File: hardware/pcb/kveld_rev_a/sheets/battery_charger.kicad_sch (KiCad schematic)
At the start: 0 parts

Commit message: feat(hw): capture rev a schematic and refine enclosure
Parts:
- added C4: 1uF 25V, Capacitor_SMD:C_0603_1608Metric, symbol Device:C
- added C5: 10uF 25V, Capacitor_SMD:C_0805_2012Metric, symbol Device:C
- added C6: 1uF 10V, Capacitor_SMD:C_0603_1608Metric, symbol Device:C
- added C7: 100nF, Capacitor_SMD:C_0603_1608Metric, symbol Device:C
- added J3: Protected LiPo + NTC, Connector_JST:JST_PH_S3B-PH-SM4-TB_1x03-1MP_P2.00mm_Horizontal, symbol Connector_Generic:Conn_01x03
- added R10, R9: 10k, Resistor_SMD:R_0603_1608Metric, symbol Device:R
- added R11: 1M, Resistor_SMD:R_0603_1608Metric, symbol Device:R
- added R12: 470k, Resistor_SMD:R_0603_1608Metric, symbol Device:R
- added R13: 100k, Resistor_SMD:R_0603_1608Metric, symbol Device:R
- added R7: 18k, Resistor_SMD:R_0603_1608Metric, symbol Device:R
- added R8: 1.20k, Resistor_SMD:R_0603_1608Metric, symbol Device:R
- added U2: BQ25185DLH, Package_DFN_QFN:Texas_DLH0010A_WSON-10-1EP_2.2x2mm_P0.4mm_EP0.9x1.5mm_ThermalVias, symbol Kveld:BQ25185DLH
- added U5: TPS22917DBVR, Package_TO_SOT_SMD:SOT-23-6, symbol Power_Management:TPS22917DBV
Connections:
- new net 3V3: R10.1, R9.1
- new net BAT_NTC: J3.2 (Pin_2), U2.6 (TS/MR)
- new net BQ_ISET: R8.1, U2.8 (ISET)
- new net BQ_VSET: R7.1, U2.7 (ILIM/VSET)
- new net CHG_ENABLE: R13.1, U2.4 (~{CE})
- new net CHG_STAT1: R9.2, U2.9 (STAT1)
- new net CHG_STAT2: R10.2, U2.3 (STAT2)
- new net GND: C4.2, C5.2, C6.2, C7.2, J3.3 (Pin_3), R12.2, R13.2, R7.2, R8.2, U2.11 (EP), U2.5 (GND), U5.2 (GND)
- new net USB_VBUS: C4.1, U2.10 (IN)
- new net VBAT: C6.1, J3.1 (Pin_1), U2.2 (BAT), U5.1 (VIN)
- new net VBAT_DIV_IN: R11.1, U5.6 (VOUT)
- new net VBAT_SENSE: C7.1, R11.2, R12.1
- new net VBAT_SENSE_EN: U5.3 (ON)
- new net VSYS: C5.1, U2.1 (SYS)
- no-connect marks 0 -> 2
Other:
- note added: "BQ25185: 4.2 V cell, 500 mA USB limit, 250 mA charge. Pack must include PCM and 10 kΩ NTC."
- title: (none) -> Battery charger, protected pack, and measurements

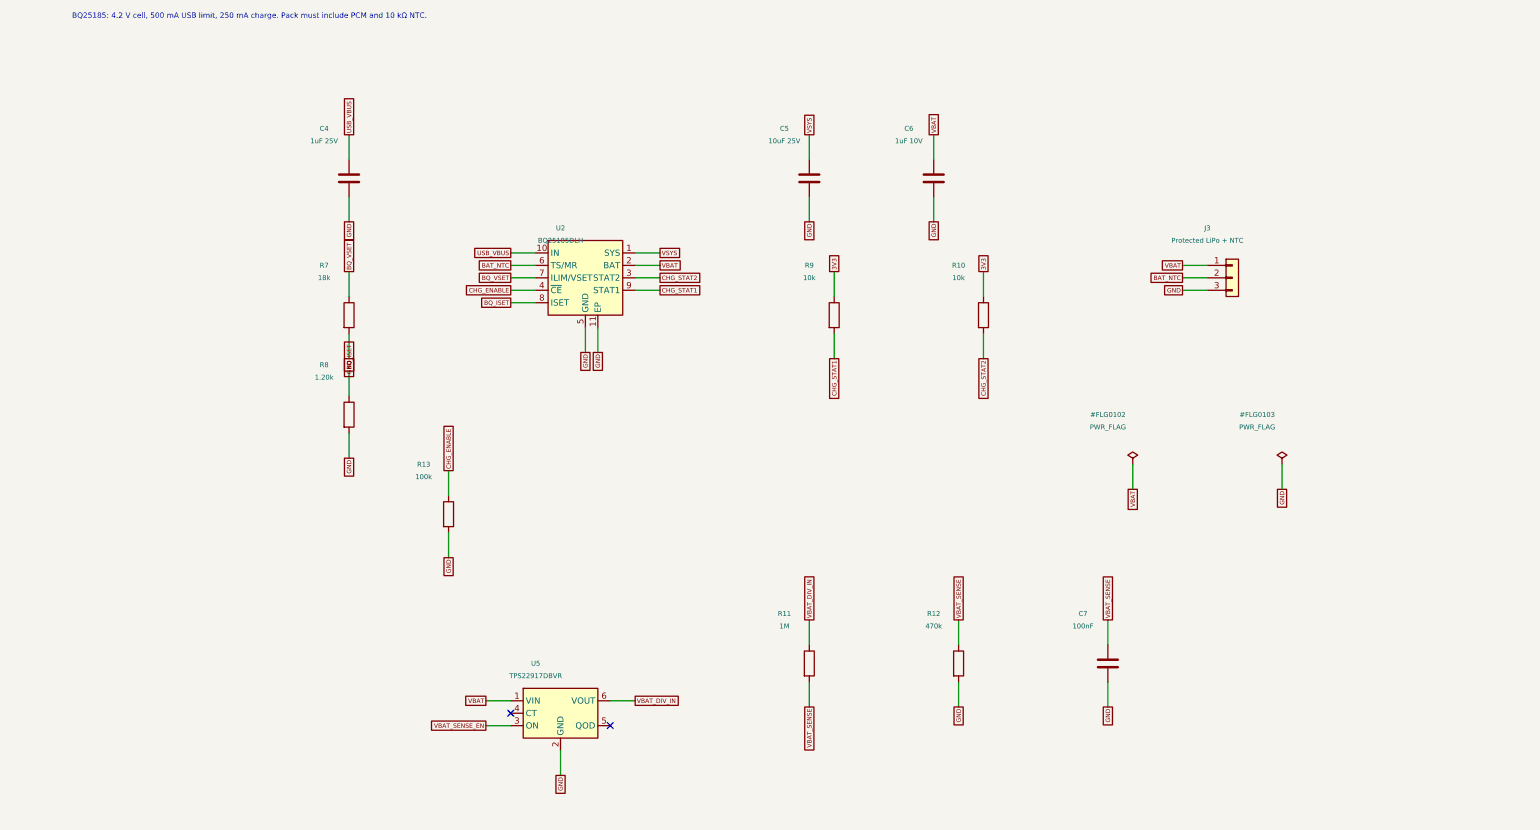
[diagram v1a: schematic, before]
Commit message: refactor(hw): consolidate and clarify schematic
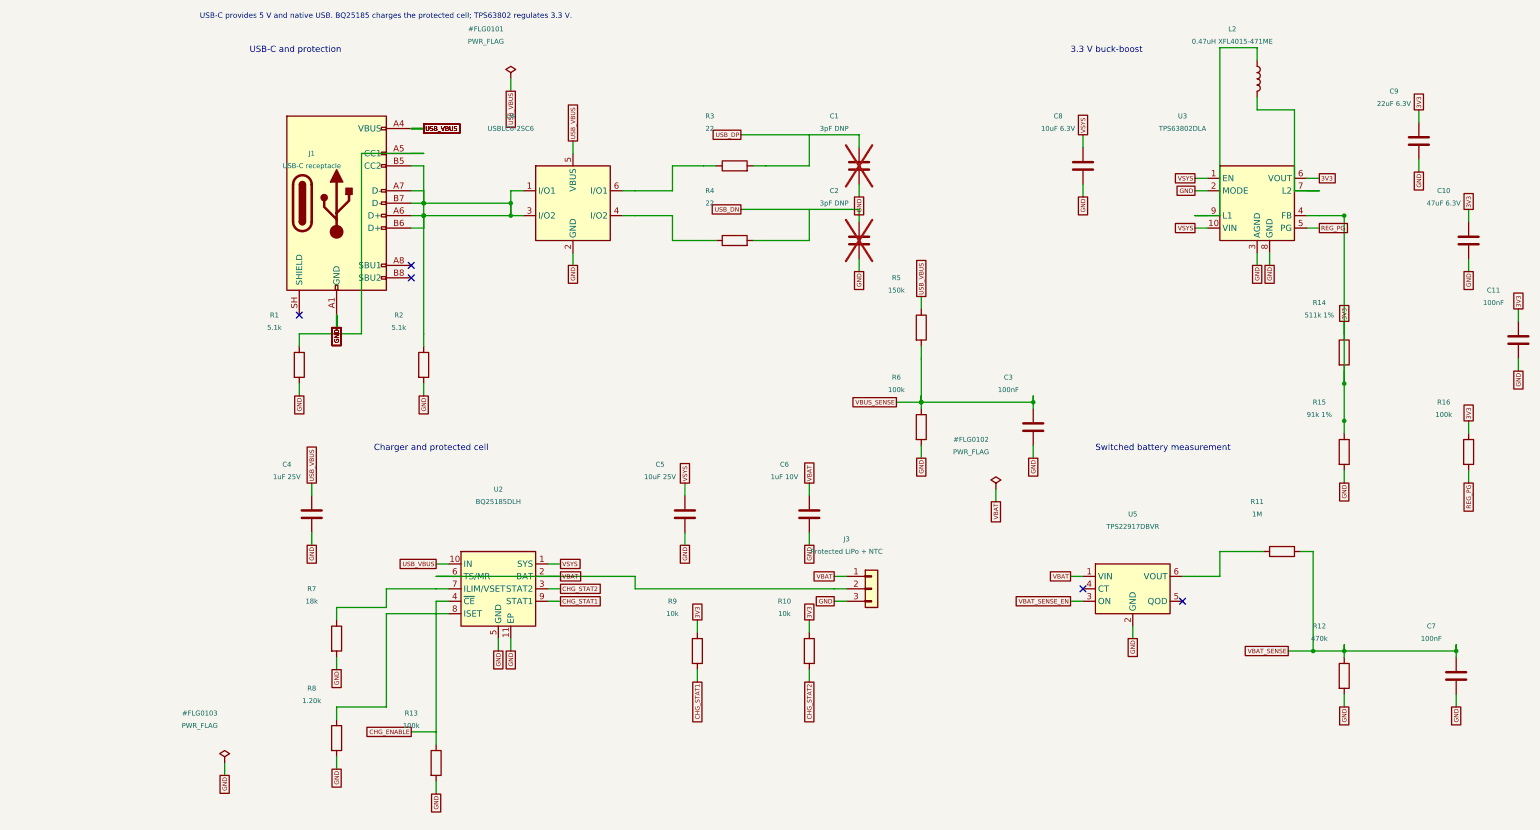
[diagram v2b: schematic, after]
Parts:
- added C1, C2: 3pF DNP, Capacitor_SMD:C_0603_1608Metric, symbol Device:C
- added C10: 47uF 6.3V, Capacitor_SMD:C_0805_2012Metric, symbol Device:C
- added C11, C3: 100nF, Capacitor_SMD:C_0603_1608Metric, symbol Device:C
- added C8: 10uF 6.3V, Capacitor_SMD:C_0603_1608Metric, symbol Device:C
- added C9: 22uF 6.3V, Capacitor_SMD:C_0603_1608Metric, symbol Device:C
- added J1: USB-C receptacle, Connector_USB:USB_C_Receptacle_HRO_TYPE-C-31-M-12, symbol Connector:USB_C_Receptacle_USB2.0_16P
- added L2: 0.47uH XFL4015-471ME, symbol Device:L
- added R1, R2: 5.1k, Resistor_SMD:R_0603_1608Metric, symbol Device:R
- added R14: 511k 1%, Resistor_SMD:R_0603_1608Metric, symbol Device:R
- added R15: 91k 1%, Resistor_SMD:R_0603_1608Metric, symbol Device:R
- added R16, R6: 100k, Resistor_SMD:R_0603_1608Metric, symbol Device:R
- added R3, R4: 22, Resistor_SMD:R_0603_1608Metric, symbol Device:R
- added R5: 150k, Resistor_SMD:R_0603_1608Metric, symbol Device:R
- added U3: TPS63802DLA, symbol Kveld:TPS63802DLA
- added U4: USBLC6-2SC6, Package_TO_SOT_SMD:SOT-23-6, symbol Kveld:USBLC6-2SC6
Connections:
- net BAT_NTC is gone; now on net VBAT: J3.2 (Pin_2), U2.6 (TS/MR)
- net 3V3: now also C10.1, C11.1, C9.1, R14.1, R14.2, R15.1, R16.1, U3.4 (FB), U3.6 (VOUT)
- net GND: now also C1.2, C10.2, C11.2, C2.2, C3.2, C8.2, C9.2, J1.A1 (GND), J1.A12 (GND), J1.B1 (GND), J1.B12 (GND), R1.2, R15.2, R2.2, R6.2, U3.2 (MODE), U3.3 (AGND), U3.8 (GND), U4.2 (GND)
- net USB_VBUS: now also J1.A4 (VBUS), J1.A9 (VBUS), J1.B4 (VBUS), J1.B9 (VBUS), R5.1, U4.5 (VBUS)
- net VSYS: now also C8.1, U3.1 (EN), U3.10 (VIN)
- net BQ_ISET: no longer names the net of R8.1, U2.8 (ISET)
- net BQ_VSET: no longer names the net of R7.1, U2.7 (ILIM/VSET)
- net VBAT_DIV_IN: no longer names the net of R11.1, U5.6 (VOUT)
- new net: R4.1, U4.4 (I/O2)
- new net: R3.1, U4.6 (I/O1)
- new net: L2.1, U3.9 (L1)
- new net: L2.2, U3.7 (L2)
- new net: J1.A5 (CC1), R1.1
- new net: J1.A6 (D+), J1.A7 (D-), J1.B5 (CC2), J1.B6 (D+), J1.B7 (D-), R2.1, U4.1 (I/O1), U4.3 (I/O2)
- new net REG_PG: R16.2, U3.5 (PG)
- new net USB_DN: C2.1, R4.2
- new net USB_DP: C1.1, R3.2
- new net VBUS_SENSE: C3.1, R5.2, R6.1
- no-connect marks 2 -> 5
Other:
- note added: "3.3 V buck-boost"
- note added: "Charger and protected cell"
- note added: "Switched battery measurement"
- note added: "USB-C and protection"
- note added: "USB-C provides 5 V and native USB. BQ25185 charges the protected cell; TPS63802 regulates 3.3 V."
- note removed: "BQ25185: 4.2 V cell, 500 mA USB limit, 250 mA charge. Pack must include PCM and 10 kΩ NTC."
- title: Battery charger, protected pack, and measurements -> Power, charging, and USB

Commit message: fix(hw): use native ground symbols
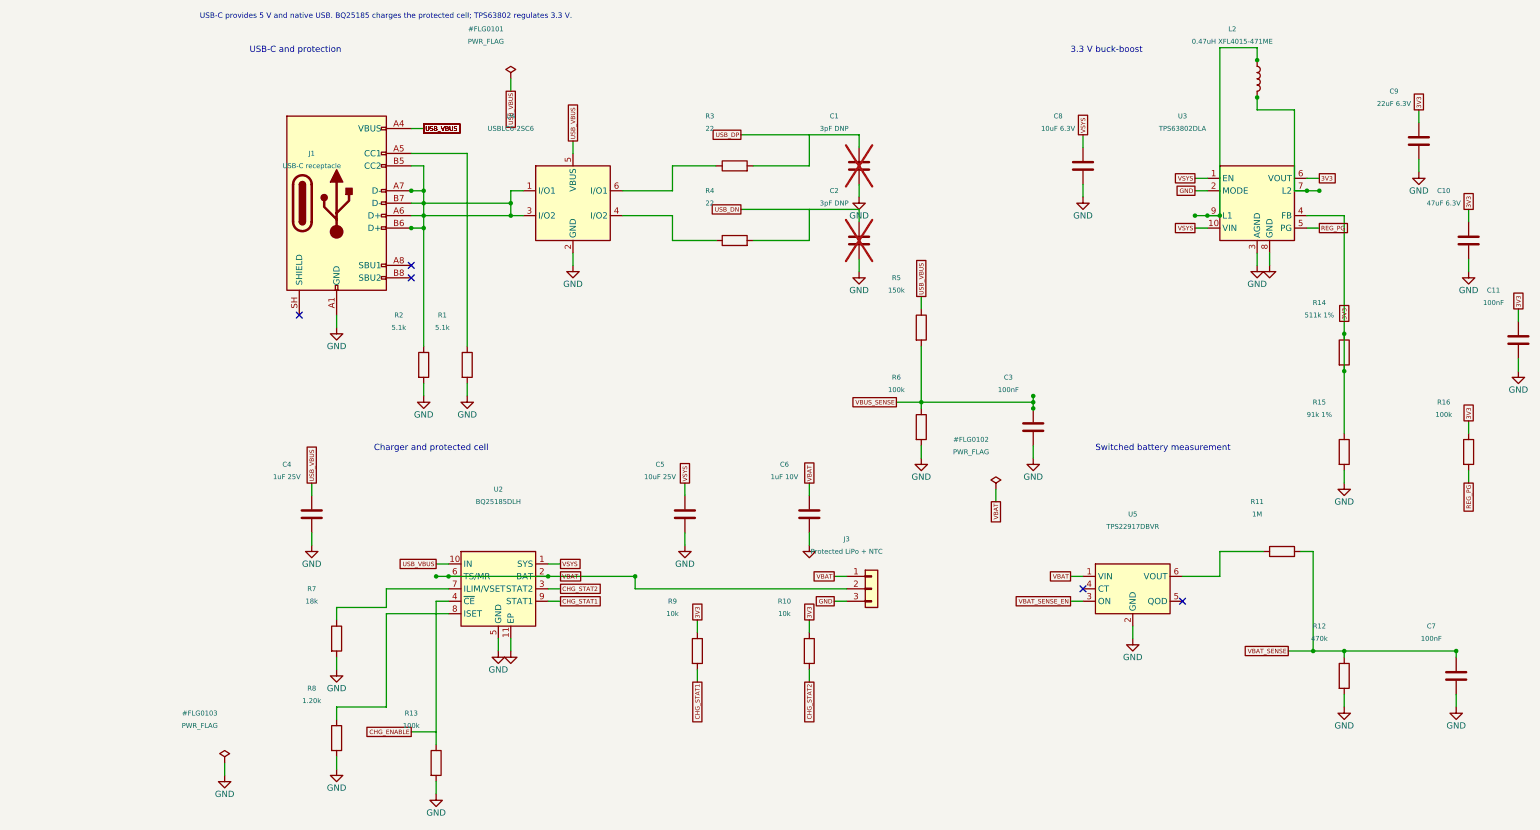
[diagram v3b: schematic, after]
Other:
- moved on the sheet: R1
